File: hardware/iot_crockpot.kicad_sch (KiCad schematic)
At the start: 17 parts, among them K1 G5LE-1, K2 G5LE-1, Q1 2N7002, Q2 2N7002, U1 AMS1117-3.3, U2 MOUDLE-SEEEDUINO-XIAO-ESP32C3, U3 MAX31855KASA

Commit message: Update firmware for XIAO ESP32-C3 and MAX31855 thermocouple
- Change build target from ESP32 to ESP32-C3 (RISC-V)
- Implement MAX31855 SPI driver replacing temperature stub
- Update GPIO assignments for XIAO ESP32-C3 pinout
- Add second relay channel (aux) for future use
- Add 10k pull-up on MAX31855 CS line in schematic
- Fix ESP-IDF 5.x component names (esp-tls, add driver/esp_timer)
- Add missing stdint.h includes for int64_t/uint8_t types
- Add firmware README and build system documentation

Co-Authored-By: Claude Opus 4.5 <noreply@anthropic.com>
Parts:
- added R3: 10k, symbol Device:R_Small_US
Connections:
- net +3V3: now also R3.1
- net at U3.6 (~{CS}): now also R3.2
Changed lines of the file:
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@@
+	)
+	(junction
+		(at 181.61 148.59)
+		(diameter 0)
+		(color 0 0 0 0)
 	)
 	(junction
@@
 	(wire
 		(pts
+			(xy 181.61 148.59) (xy 181.61 146.05)
+		)
+		(stroke
+			(width 0)
+			(type default)
+		)
+	)
+	(wire
+		(pts
 			(xy 191.77 134.62) (xy 199.39 134.62)
 		)
@@
 	(wire
 		(pts
+			(xy 167.64 148.59) (xy 181.61 148.59)
+		)
+		(stroke
+			(width 0)
+			(type default)
+		)
+	)
+	(wire
+		(pts
+			(xy 181.61 148.59) (xy 184.15 148.59)
+		)
+		(stroke
+			(width 0)
+			(type default)
+		)
+	)
+	(wire
+		(pts
 			(xy 228.6 81.28) (xy 228.6 72.39)
 		)
@@
 		(pts
 			(xy 199.39 137.16) (xy 199.39 134.62)
+		)
+		(stroke
+			(width 0)
+			(type default)
+		)
+	)
+	(wire
+		(pts
+			(xy 181.61 138.43) (xy 181.61 140.97)
 		)
 		(stroke
@@
 	)
 	(symbol
+		(lib_id "Device:R_Small_US")
+		(at 181.61 143.51 0)
+		(unit 1)
+		(exclude_from_sim no)
+		(in_bom yes)
+		(on_board yes)
+		(dnp no)
+		(property "Reference" "R3"
+			(at 177.292 142.24 0)
+			(effects
+				(font
+					(size 1.27 1.27)
+				)
+				(justify left)
+			)
+		)
+		(property "Value" "10k"
+			(at 176.276 144.78 0)
+			(effects
+				(font
+					(size 1.27 1.27)
+				)
+				(justify left)
+			)
+		)
+		(property "Footprint" ""
+			(at 181.61 143.51 0)
+			(effects
+				(font
+					(size 1.27 1.27)
+				)
+				(hide yes)
+			)
+		)
+		(property "Datasheet" "~"
+			(at 181.61 143.51 0)
+			(effects
+				(font
+					(size 1.27 1.27)
+				)
+				(hide yes)
+			)
+		)
+		(property "Description" "Resistor, small US symbol"
+			(at 181.61 143.51 0)
+			(effects
+				(font
+					(size 1.27 1.27)
+				)
+				(hide yes)
+			)
+		)
+		(pin "1"
+		)
+		(pin "2"
+		)
+		(instances
+			(project "iot_crockpot"
+				(path "/00000000-0000-0000-0000-000000000001"
+					(reference "R3")
+					(unit 1)
+				)
+			)
+		)
+	)
+	(symbol
 		(lib_id "power:+5V")
 		(at 248.92 114.3 0)
@@
 					(unit 1)
 				)
+			)
+		)
+	)
+	(symbol
+		(lib_id "power:+3V3")
+		(at 181.61 138.43 0)
+		(unit 1)
+		(exclude_from_sim no)
+		(in_bom yes)
+		(on_board yes)
+		(dnp no)
+		(fields_autoplaced yes)
+		(property "Reference" "#PWR012"
+			(at 181.61 142.24 0)
+			(effects
+				(font
+					(size 1.27 1.27)
+				)
+				(hide yes)
+			)
+		)
+		(property "Value" "+3V3"
+			(at 181.61 133.35 0)
+			(effects
+				(font
+					(size 1.27 1.27)
+				)
+			)
+		)
+		(property "Footprint" ""
+			(at 181.61 138.43 0)
+			(effects
+				(font
+					(size 1.27 1.27)
+				)
+				(hide yes)
+			)
+		)
+		(property "Datasheet" ""
+			(at 181.61 138.43 0)
+			(effects
+				(font
+					(size 1.27 1.27)
+				)
+				(hide yes)
+			)
+		)
+		(property "Description" "Power symbol creates a global label with name \"+3V3\""
+			(at 181.61 138.43 0)
+			(effects
+				(font
+					(size 1.27 1.27)
+				)
+				(hide yes)
+			)
+		)
+		(pin "1"
+		)
+		(instances
+			(project "iot_crockpot"
+				(path "/00000000-0000-0000-0000-000000000001"
+					(reference "#PWR012")
+					(unit 1)
+				)

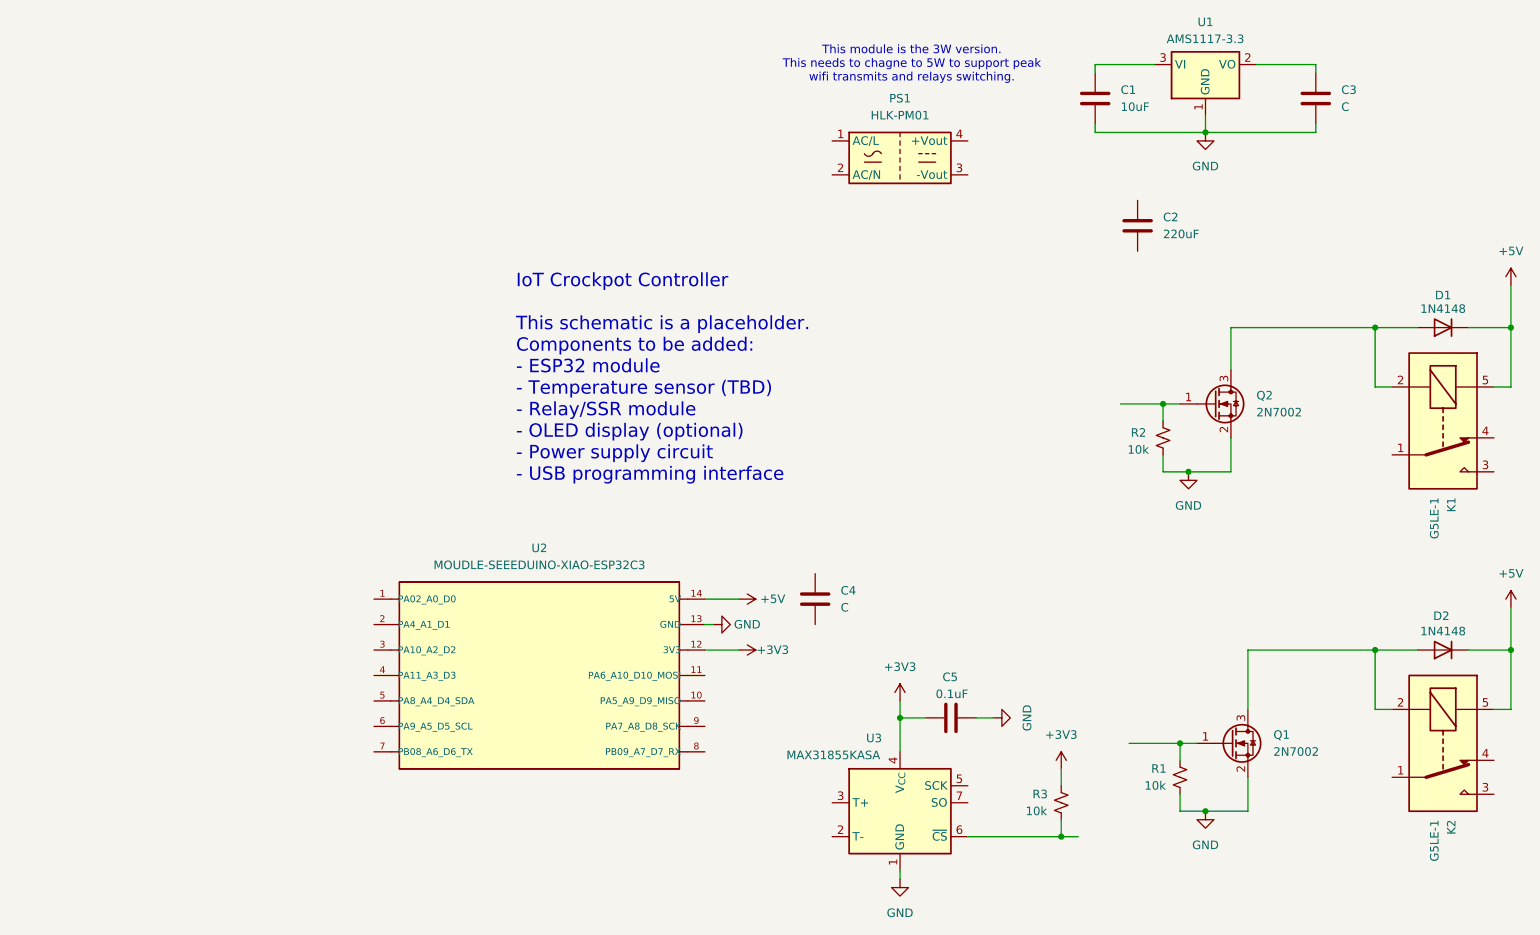
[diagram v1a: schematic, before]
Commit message: Add CYD enclosure design and remote control features
Hardware:
- Add OpenSCAD enclosure design for ESP32-3248S035C (CYD 3.5")
- Angled display with isolation barrier for relay section
- Socket for crockpot switch cylinder mount
- Add display comparison spreadsheet for hardware selection

Simulator:
- Add Telegram bot for remote control
- Add web server interface
- Add remote control manager to coordinate services
- Update main.py with GUI integration and view modes
- Add .env.example for configuration

Co-Authored-By: Claude Opus 4.5 <noreply@anthropic.com>
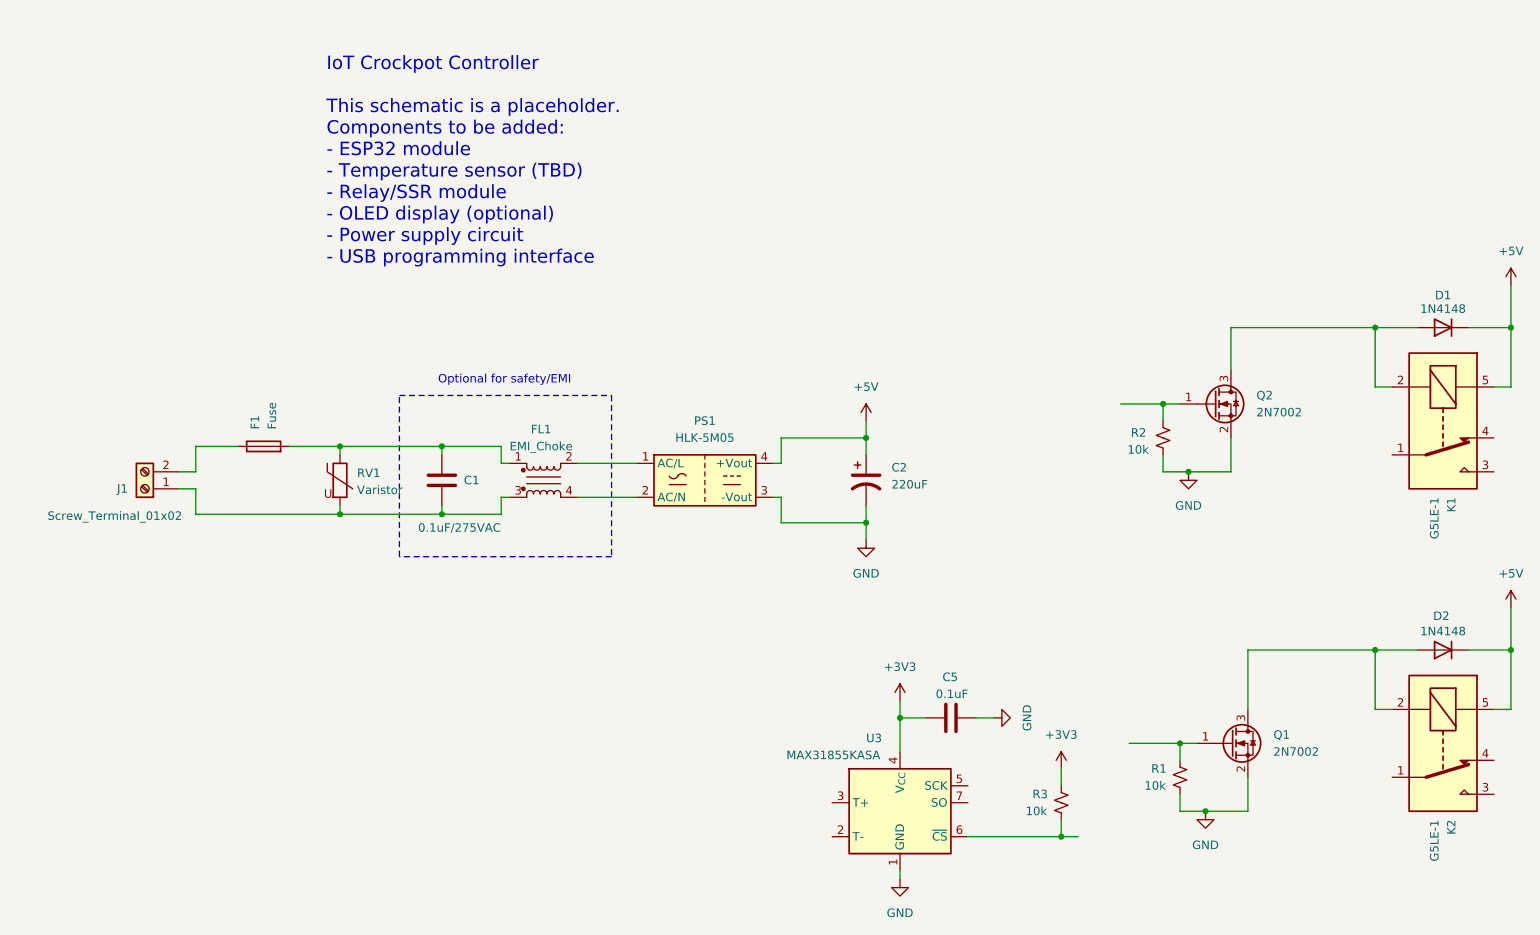
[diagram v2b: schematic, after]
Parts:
- removed C2: 220uF, symbol Device:C
- removed C3, C4: C, symbol Device:C
- removed PS1: HLK-PM01, Converter_ACDC:Converter_ACDC_Hi-Link_HLK-PMxx, symbol Converter_ACDC:HLK-PM01
- removed U1: AMS1117-3.3, Package_TO_SOT_SMD:SOT-223-3_TabPin2, symbol Regulator_Linear:AMS1117-3.3
- removed U2: MOUDLE-SEEEDUINO-XIAO-ESP32C3, XIAO-ESP32-C3:MCU_Seeed_ESP32C3_w_3D_model, symbol MOUDLE-SEEEDUINO-XIAO-ESP32C3:MOUDLE-SEEEDUINO-XIAO-ESP32C3
- added C2: 220uF, symbol Device:C_Polarized_US
- added F1: Fuse, symbol Device:Fuse
- added FL1: EMI_Choke, symbol Device:Filter_EMI_CommonMode
- added J1: Screw_Terminal_01x02, symbol Connector:Screw_Terminal_01x02
- added PS1: HLK-5M05, Converter_ACDC:Converter_ACDC_Hi-Link_HLK-5Mxx, symbol Converter_ACDC:HLK-5M05
- added RV1: Varistor, symbol Device:Varistor
- C1: value 10uF -> 0.1uF/275VAC
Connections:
- net +5V: now also C2.1, PS1.4 (+Vout)
- net GND: now also C2.2, PS1.3 (-Vout); no longer C1.2
- net at C1.1: now also F1.2, FL1.1, RV1.1
- new net: C1.2, FL1.3, J1.1 (Pin_1), RV1.2
- new net: F1.1, J1.2 (Pin_2)
- new net: FL1.2, PS1.1 (AC/L)
- new net: FL1.4, PS1.2 (AC/N)
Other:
- note added: "Optional for safety/EMI"
- note removed: "This module is the 3W version. This needs to chagne to 5W to support peak wifi transmits and relays switching."
